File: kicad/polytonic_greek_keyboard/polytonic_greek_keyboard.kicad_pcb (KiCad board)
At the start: 2 copper layers, 34 parts, among them J1 PINHD_1x4_Male, J2 USB_C_Receptacle, J3 PINHD_1x2_Male, Q1 S8050, SW1 SW_Wuerth_450301014042, SW2 RotaryEncoder_Switch_MP, SW4 SW_SP4T_NR01104, SW5 SW_SPST, U1 ESP32-S2-WROVER, U2 PCF8574T

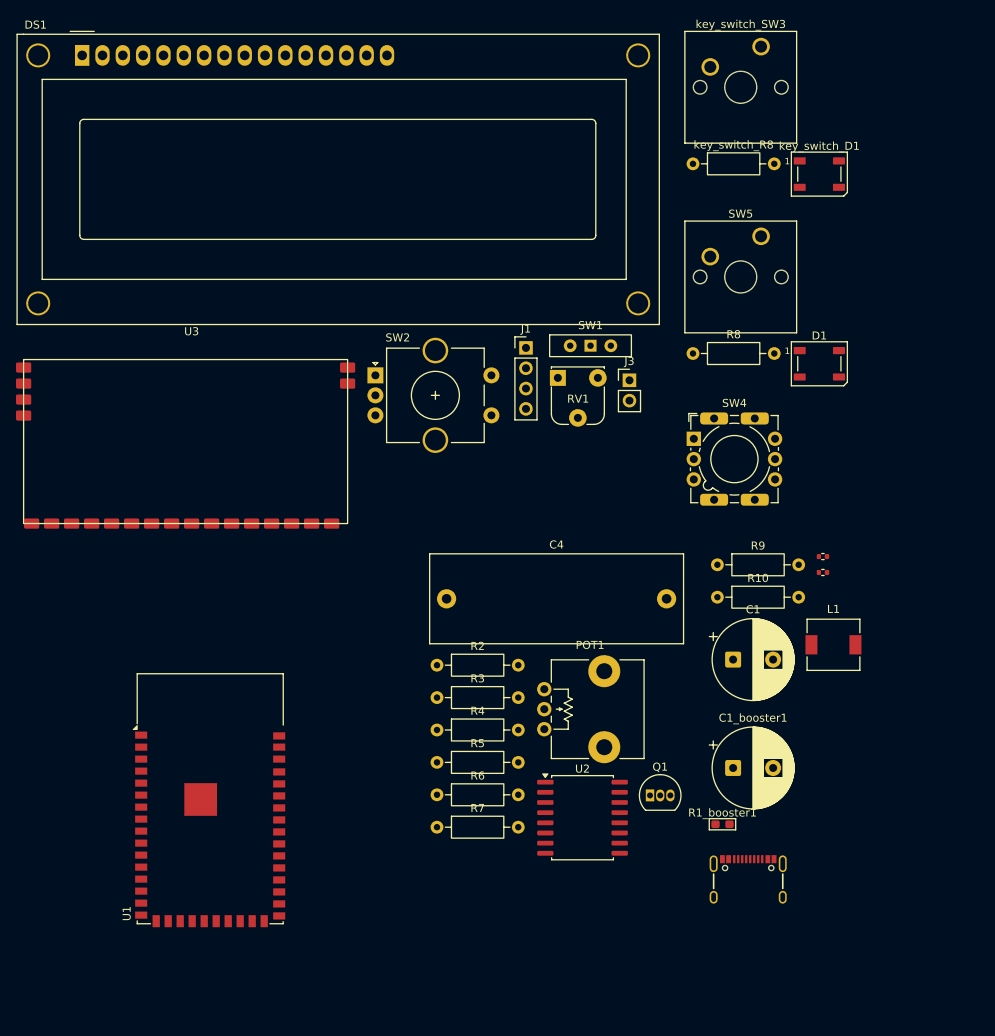
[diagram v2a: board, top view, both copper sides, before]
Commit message: [ADD] a more structured approach of the pcb in a way that won't overload the esp32 that is running it
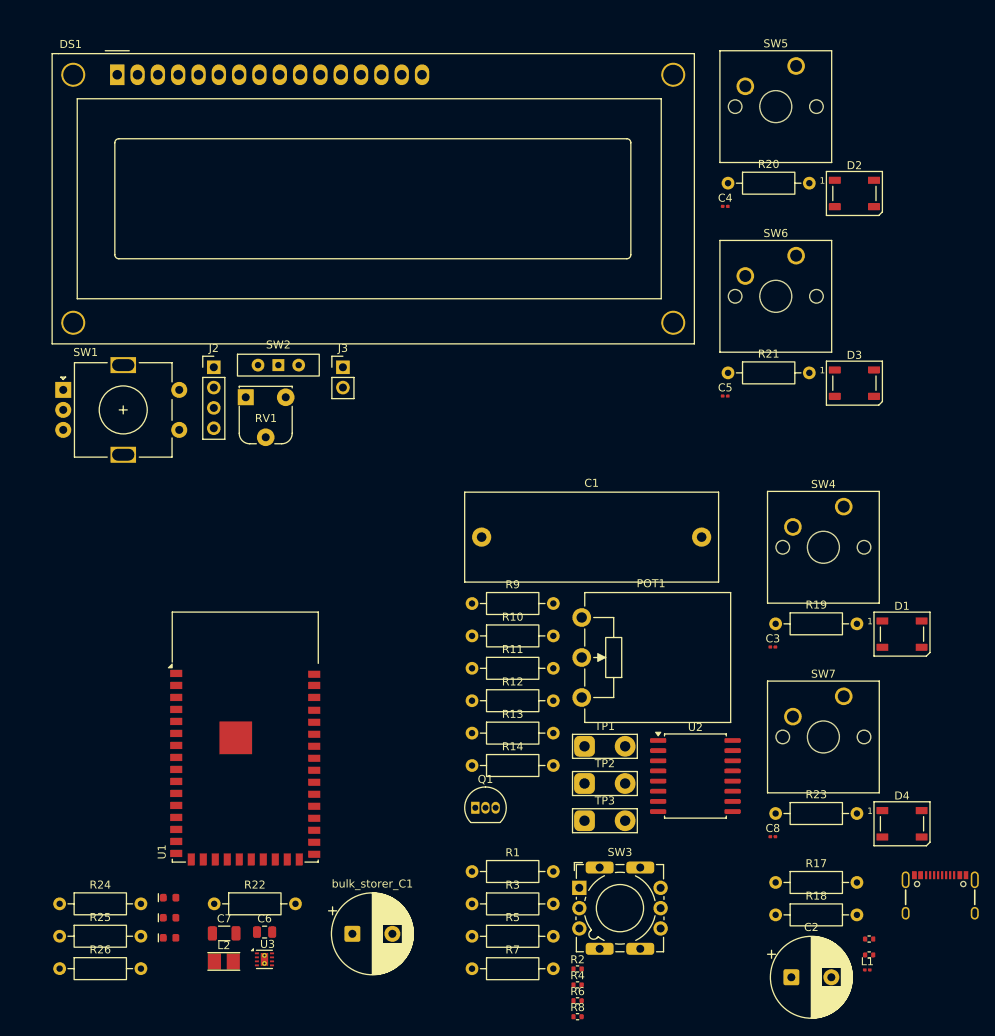
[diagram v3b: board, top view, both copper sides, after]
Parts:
- removed C1_booster1: 1000uF_16V, Capacitor_THT:CP_Radial_D10.0mm_P5.00mm
- removed R1_booster1: 330R_0603, PCM_Resistor_SMD_AKL:R_0603_1608Metric_Pad1.05x0.95mm_HandSolder
- removed key_switch_D1: WS2812B, LED_SMD:LED_WS2812B_PLCC4_5.0x5.0mm_P3.2mm
- removed key_switch_R8: 330ohm, Resistor_THT:R_Axial_DIN0207_L6.3mm_D2.5mm_P10.16mm_Horizontal
- removed key_switch_SW3: SW_SPST, Button_Switch_Keyboard:SW_Cherry_MX_1.00u_PCB
- added C2: 1000uF_16V, Capacitor_THT:CP_Radial_D10.0mm_P5.00mm, F.Cu at (114.1, 135.0)
- added C3: 0.1uF_0603_16V, Capacitor_SMD:C_0201_0603Metric, F.Cu at (111.8, 93.7)
- added C5: 0.1uF_0603_16V, Capacitor_SMD:C_0201_0603Metric, F.Cu at (105.8, 62.4)
- added C6: 10uF_0805_16V_lowESR, Capacitor_SMD:C_0805_2012Metric, F.Cu at (48.2, 129.4)
- added C7: 22uF_1206_25V, Capacitor_SMD:C_1206_3216Metric, F.Cu at (43.2, 129.5)
- added C8: 0.1uF_0603_16V, Capacitor_SMD:C_0201_0603Metric, F.Cu at (111.8, 117.4)
- added D2: WS2812B, LED_SMD:LED_WS2812B_PLCC4_5.0x5.0mm_P3.2mm, F.Cu at (122.0, 37.0)
- added D3: WS2812B, LED_SMD:LED_WS2812B_PLCC4_5.0x5.0mm_P3.2mm, F.Cu at (122.0, 60.7)
- added D4: WS2812B, LED_SMD:LED_WS2812B_PLCC4_5.0x5.0mm_P3.2mm, F.Cu at (127.9, 115.8)
- added D5: Green, PCM_SparkFun-LED:LED_0603_1608Metric_Green, F.Cu at (36.4, 125.1)
- added D6: Green, PCM_SparkFun-LED:LED_0603_1608Metric_Green, F.Cu at (36.4, 127.6)
- added D7: Green, PCM_SparkFun-LED:LED_0603_1608Metric_Green, F.Cu at (36.4, 130.1)
- added L2: 2.2uH_2.4A_2016, Inductor_SMD:L_Taiyo-Yuden_NR-20xx_HandSoldering, F.Cu at (43.1, 133.0)
- added R1: 330ohm, Resistor_THT:R_Axial_DIN0207_L6.3mm_D2.5mm_P10.16mm_Horizontal, F.Cu at (74.2, 121.8)
- added R13: 47k, Resistor_THT:R_Axial_DIN0207_L6.3mm_D2.5mm_P10.16mm_Horizontal, F.Cu at (74.2, 104.5)
- added R14: 47k, Resistor_THT:R_Axial_DIN0207_L6.3mm_D2.5mm_P10.16mm_Horizontal, F.Cu at (74.2, 108.5)
- added R15: 5.1k, PCM_SparkFun-Resistor:R_0402_1005Metric, F.Cu at (123.8, 130.2)
- added R16: 5.1k, PCM_SparkFun-Resistor:R_0402_1005Metric, F.Cu at (123.8, 132.2)
- added R17: 22ohm, Resistor_THT:R_Axial_DIN0207_L6.3mm_D2.5mm_P10.16mm_Horizontal, F.Cu at (112.1, 123.2)
- added R18: 22ohm, Resistor_THT:R_Axial_DIN0207_L6.3mm_D2.5mm_P10.16mm_Horizontal, F.Cu at (112.1, 127.2)
- added R19: 330ohm, Resistor_THT:R_Axial_DIN0207_L6.3mm_D2.5mm_P10.16mm_Horizontal, F.Cu at (112.1, 90.8)
- added R20: 330ohm, Resistor_THT:R_Axial_DIN0207_L6.3mm_D2.5mm_P10.16mm_Horizontal, F.Cu at (106.2, 35.7)
- added R21: 330ohm, Resistor_THT:R_Axial_DIN0207_L6.3mm_D2.5mm_P10.16mm_Horizontal, F.Cu at (106.2, 59.5)
- added R22: 100k, Resistor_THT:R_Axial_DIN0207_L6.3mm_D2.5mm_P10.16mm_Horizontal, F.Cu at (41.9, 125.8)
- added R23: 330ohm, Resistor_THT:R_Axial_DIN0207_L6.3mm_D2.5mm_P10.16mm_Horizontal, F.Cu at (112.1, 114.5)
- added R24: 68ohm, Resistor_THT:R_Axial_DIN0207_L6.3mm_D2.5mm_P10.16mm_Horizontal, F.Cu at (22.6, 125.8)
- added R25: 220ohm, Resistor_THT:R_Axial_DIN0207_L6.3mm_D2.5mm_P10.16mm_Horizontal, F.Cu at (22.6, 129.9)
- added R26: 68ohm, Resistor_THT:R_Axial_DIN0207_L6.3mm_D2.5mm_P10.16mm_Horizontal, F.Cu at (22.6, 133.9)
- added SW3: SW_SP4T_NR01104, Button_Switch_THT:SW_NKK_NR01, F.Cu at (87.6, 123.8)
- added SW6: SW_SPST, Button_Switch_Keyboard:SW_Cherry_MX_1.00u_PCB, F.Cu at (114.7, 44.8)
- added SW7: SW_SPST, Button_Switch_Keyboard:SW_Cherry_MX_1.00u_PCB, F.Cu at (120.6, 99.9)
- added TP1: TestPoint_2Pole, Misc:TestPoint_2Pads_Pitch5.08mm_Drill1.3mm, F.Cu at (88.2, 106.1)
- added TP2: TestPoint_2Pole, Misc:TestPoint_2Pads_Pitch5.08mm_Drill1.3mm, F.Cu at (88.2, 110.8)
- added TP3: TestPoint_2Pole, Misc:TestPoint_2Pads_Pitch5.08mm_Drill1.3mm, F.Cu at (88.2, 115.4)
- added bulk_storer_C1: 1000uF_16V, Capacitor_THT:CP_Radial_D10.0mm_P5.00mm, F.Cu at (59.2, 129.6)
- C1: value 1000uF_16V -> 0.1uF; footprint Capacitor_THT:CP_Radial_D10.0mm_P5.00mm -> Capacitor_THT:C_Rect_L31.5mm_W11.0mm_P27.50mm_MKS4
- C4: value 0.1uF -> 0.1uF_0603_16V; footprint Capacitor_THT:C_Rect_L31.5mm_W11.0mm_P27.50mm_MKS4 -> Capacitor_SMD:C_0201_0603Metric
- J1: value PINHD_1x4_Male -> USB_C_Receptacle; footprint Connector_PinHeader_2.54mm:PinHeader_1x04_P2.54mm_Vertical -> PCM_SparkFun-Connector:USB-C_16
- J2: value USB_C_Receptacle -> PINHD_1x4_Male; footprint PCM_SparkFun-Connector:USB-C_16 -> Connector_PinHeader_2.54mm:PinHeader_1x04_P2.54mm_Vertical
- L1: footprint Inductor_SMD:L_6.3x6.3_H3 -> Inductor_SMD:L_0201_0603Metric
- POT1: footprint PCM_Potentiometer_THT_US_AKL:Potentiometer_Alps_RK09L_Single_Vertical -> Misc:Potentiometer_Piher_PC-16_Single_Vertical
- R10, R9: value 22ohm -> 1k
- R11: value 5.1k -> 47k; footprint PCM_SparkFun-Resistor:R_0402_1005Metric -> Resistor_THT:R_Axial_DIN0207_L6.3mm_D2.5mm_P10.16mm_Horizontal
- R12: value 5.1k -> 1k; footprint PCM_SparkFun-Resistor:R_0402_1005Metric -> Resistor_THT:R_Axial_DIN0207_L6.3mm_D2.5mm_P10.16mm_Horizontal
- R2, R6: value 47k -> 10k_0402; footprint Resistor_THT:R_Axial_DIN0207_L6.3mm_D2.5mm_P10.16mm_Horizontal -> Resistor_SMD:R_0402_1005Metric
- R3, R5: value 1k -> 330ohm
- R4: value 1k -> 10k_0402; footprint Resistor_THT:R_Axial_DIN0207_L6.3mm_D2.5mm_P10.16mm_Horizontal -> Resistor_SMD:R_0402_1005Metric
- R7: value 47k -> 330ohm
- R8: value 330ohm -> 10k_0402; footprint Resistor_THT:R_Axial_DIN0207_L6.3mm_D2.5mm_P10.16mm_Horizontal -> Resistor_SMD:R_0402_1005Metric
- SW1: value SW_Wuerth_450301014042 -> RotaryEncoder_Switch_MP; footprint Button_Switch_THT:SW_Slide-03_Wuerth-WS-SLTV_10x2.5x6.4_P2.54mm -> Misc:RotaryEncoder_Alps_EC11E-Switch_Vertical_H20mm
- SW2: value RotaryEncoder_Switch_MP -> SW_Wuerth_450301014042; footprint Rotary_Encoder:RotaryEncoder_Alps_EC11E-Switch_Vertical_H20mm_CircularMountingHoles -> Button_Switch_THT:SW_Slide-03_Wuerth-WS-SLTV_10x2.5x6.4_P2.54mm
- SW4: value SW_SP4T_NR01104 -> SW_SPST; footprint Button_Switch_THT:SW_NKK_NR01 -> Button_Switch_Keyboard:SW_Cherry_MX_1.00u_PCB
- U3: value ~ -> TPS62162DSG; footprint polytonic_greek_keyboard:I²C -> Package_SON:WSON-8-1EP_2x2mm_P0.5mm_EP0.9x1.6mm_ThermalVias
- moved J2 90.6 mm to (41.9, 58.8)
- moved R8 84.1 mm to (87.4, 139.9)
- moved J1 83.5 mm to (132.7, 121.9)
- moved U3 78.5 mm to (48.2, 132.8)
- moved SW1 66.1 mm to (23.1, 61.6)
- moved C4 60.2 mm to (105.8, 38.6)
- moved R12 46.7 mm to (74.2, 100.4)
- moved R11 46.0 mm to (74.2, 96.4)
- moved R2 41.8 mm to (87.4, 134.0)
- moved L1 40.9 mm to (123.6, 134.1)
- moved RV1 39.1 mm to (48.4, 64.5)
- moved R4 36.4 mm to (87.4, 136.0)
- moved J3 35.9 mm to (58.0, 58.8)
- moved D1 35.3 mm to (127.9, 92.1)
- moved C1 35.0 mm to (75.4, 80.0)
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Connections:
- net /key_alpha/switch_column renamed /key_matrix/Alphabet keys/col1_IN
- net /logic/ID01 renamed /key_matrix/row8_IN
- net /logic/ID03 renamed /key_matrix/row6_IN
- net /logic/ID04 renamed /key_matrix/row5_IN
- net /logic/ID05 renamed /key_matrix/row4_IN
- net /logic/ID06 renamed /key_matrix/row3_IN
- net /logic/ID07 renamed /key_matrix/row2_IN
- net /logic/ID08 renamed /key_matrix/row1_IN
- net /system_speech/VSS - LINUX renamed /key_matrix/Return/swt_col
- C1 pad 1: /power_filter/GND_IN -> VCC
- C1 pad 2: /power_filter/VBUS_OUT -> GND
- C4 pad 1: VCC -> /esp_voltage_stepdown/VDD_CLEAN
- C4 pad 2: GND -> Net-(D2-VDD)
- D1 pad 2: /key_alpha/LED_DOUT -> /key_matrix/Navigation keys/LED_DIN_IN
- D1 pad 3: /key_alpha/LED_VSS -> GND
- DS1 pad 1: Net-(DS1-VSS) -> GND
- DS1 pad 10: unconnected-(DS1-D3-Pad10) -> /display/Onboard_I2c/DB3
- DS1 pad 11: Net-(DS1-D4) -> /display/Onboard_I2c/DB4
- DS1 pad 12: Net-(DS1-D5) -> /display/Onboard_I2c/DB5
- DS1 pad 13: Net-(DS1-D6) -> /display/Onboard_I2c/DB6
- DS1 pad 14: Net-(DS1-D7) -> /display/Onboard_I2c/DB7
- DS1 pad 15: Net-(DS1-LED(+)) -> GND
- DS1 pad 16: Net-(DS1-LED(-)) -> /display/Onboard_I2c/(K) BL-
- DS1 pad 2: Net-(DS1-VDD) -> VCC
- DS1 pad 3: Net-(DS1-VO) -> /display/Onboard_I2c/V0
- DS1 pad 4: Net-(DS1-RS) -> /display/Onboard_I2c/RS
- DS1 pad 5: Net-(DS1-R/W) -> /display/Onboard_I2c/R/W
- DS1 pad 6: Net-(DS1-E) -> /display/Onboard_I2c/E
- DS1 pad 7: unconnected-(DS1-D0-Pad7) -> /display/Onboard_I2c/DB0
- DS1 pad 8: unconnected-(DS1-D1-Pad8) -> /display/Onboard_I2c/DB1
- DS1 pad 9: unconnected-(DS1-D2-Pad9) -> /display/Onboard_I2c/DB2
- J3 pad 2: Net-(U3-LED_VCC) -> VCC
- L1 pad 1: /power_filter/GND_IN -> GND
- L1 pad 2: /power_filter/VBUS_OUT -> /esp_voltage_stepdown/VDD_CLEAN
- R10 pad 1: /power_filter/DATA-_IN -> VCC
- R10 pad 2: /power_filter/DATA-_OUT -> /display/Onboard_I2c/A1
- R11 pad 1: /power_filter/CC1_IN -> /display/SDA
- R11 pad 2: /power_filter/GND_IN -> VCC
- R12 pad 1: /power_filter/CC2_IN -> VCC
- R12 pad 2: /power_filter/GND_IN -> /display/Onboard_I2c/A2
- R2 pad 1: VCC -> /logic/ID41
- R2 pad 2: Net-(Q1-B) -> /display/VCC_SCREEN
- R3 pad 1: VCC -> Net-(R3-Pad1)
- R3 pad 2: /display/Onboard_I2c/A0 -> /logic/ID45
- R4 pad 1: VCC -> /logic/ID45
- R4 pad 2: /display/Onboard_I2c/A1 -> /display/VCC_SCREEN
- R5 pad 1: VCC -> /logic/ID46
- R5 pad 2: /display/Onboard_I2c/A2 -> Net-(R5-Pad2)
- R6 pad 1: /display/Onboard_I2c/SCL -> /logic/ID46
- R6 pad 2: VCC -> /display/VCC_SCREEN
- R7 pad 1: /display/Onboard_I2c/SDA -> /logic/ID42
- R7 pad 2: VCC -> Net-(R7-Pad2)
- R8 pad 1: Net-(D1-DIN) -> /logic/ID42
- R8 pad 2: /key_alpha/LED_DIN -> /display/VCC_SCREEN
- R9 pad 1: /power_filter/DATA+_IN -> VCC
- R9 pad 2: /power_filter/DATA+_OUT -> /display/Onboard_I2c/A0
- RV1 pad 1: Net-(U3-LED_VCC) -> VCC
- RV1 pad 3: Net-(SW1-C) -> VCC
- SW4 pad 1: /system_speech/VSS - RAW -> /key_matrix/row7_IN
- SW5 pad 1: /key_alpha/switch_row -> /key_matrix/row9_IN
- U1 pad 1: /logic/GND -> GND
- U1 pad 12: /logic/ID09 -> /key_matrix/LED_DIN
- U1 pad 13: /logic/ID10 -> /display/SDA
- U1 pad 14: /logic/ID11 -> /display/SCL
- U1 pad 2: /logic/3v3 -> /display/VCC_SCREEN
- U1 pad 26: /logic/GND -> GND
- U1 pad 3: /logic/ID00 -> /key_matrix/row9_IN
- U1 pad 42: /logic/GND -> GND
- U1 pad 43: /logic/GND -> GND
- U1 pad 5: /logic/ID02 -> /key_matrix/row7_IN
- U2 pad 1: /display/Onboard_I2c/A0 -> unconnected-(U2-A0-Pad1)
- U2 pad 10: /display/Onboard_I2c/DB5 -> /display/Onboard_I2c/DB4
- U2 pad 11: /display/Onboard_I2c/DB6 -> /display/Onboard_I2c/DB5
- U2 pad 12: /display/Onboard_I2c/DB7 -> /display/Onboard_I2c/DB6
- U2 pad 14: /display/Onboard_I2c/SCL -> unconnected-(U2-SCL-Pad14)
- U2 pad 15: /display/Onboard_I2c/SDA -> /display/SCL
- U2 pad 2: /display/Onboard_I2c/A1 -> /display/Onboard_I2c/A0
- U2 pad 3: /display/Onboard_I2c/A2 -> /display/Onboard_I2c/A1
- U2 pad 4: /display/Onboard_I2c/RS -> unconnected-(U2-P0-Pad4)
- U2 pad 5: /display/Onboard_I2c/R/W -> /display/Onboard_I2c/RS
- U2 pad 6: /display/Onboard_I2c/E -> /display/Onboard_I2c/R/W
- U2 pad 7: Net-(Q1-B) -> /display/Onboard_I2c/E
- U2 pad 8: GND -> unconnected-(U2-GND-Pad8)
- U2 pad 9: /display/Onboard_I2c/DB4 -> Net-(Q1-B)
- U3 pad 2: Net-(DS1-VDD) -> GND
- U3 pad 3: /display/SDA -> GND
- U3 pad 4: /display/SCL -> GND
- U3 pad 5: Net-(DS1-R/W) -> GND
- U3 pad 7: unconnected-(U3-DB0-Pad7) -> Net-(U3-SW)
- U3 pad 8: unconnected-(U3-DB1-Pad8) -> Net-(U3-PG)
- U3 pad 9: unconnected-(U3-DB2-Pad9) -> GND

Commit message: [UPDATE] the board desing, [FIX] connection issues
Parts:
- added C9: 100nF_Ceramic, Capacitor_THT:C_Disc_D5.0mm_W2.5mm_P2.50mm, F.Cu at (75.2, 93.7)
- added D8: Blue, PCM_SparkFun-LED:LED_1206_3216Metric_Blue, F.Cu at (181.4, 132.2)
- added J4: Conn_01x11_Socket, Connector_PinSocket_2.00mm:PinSocket_1x11_P2.00mm_Horizontal, F.Cu at (197.5, 102.5)
- added J5: Conn_01x11_Pin, Connector_PinHeader_2.00mm:PinHeader_1x11_P2.00mm_Horizontal, F.Cu at (180.6, 102.5)
- added R27: 10k_0402, Resistor_SMD:R_0402_1005Metric, F.Cu at (81.2, 92.6)
- added R28: 10k_0402, Resistor_SMD:R_0402_1005Metric, F.Cu at (81.2, 94.6)
- added R29: 1k, Resistor_THT:R_Axial_DIN0207_L6.3mm_D2.5mm_P10.16mm_Horizontal, F.Cu at (180.2, 128.6)
- added SW8: Push_Button, Button_Switch_THT:SW_PUSH_6mm, F.Cu at (75.2, 76.6)
- added SW9: Push_Button, Button_Switch_THT:SW_PUSH_6mm, F.Cu at (75.2, 85.1)
- added U4: MCP23017_SP, Package_DIP:DIP-28_W7.62mm, F.Cu at (108.8, 21.5)
- added U5: MCP23017_SP, Package_DIP:DIP-28_W7.62mm, F.Cu at (119.5, 21.5)
- C3, C4, C5, C8: footprint Capacitor_SMD:C_0201_0603Metric -> Capacitor_SMD:C_0201_0603Metric_Pad0.64x0.40mm_HandSolder
- C6: footprint Capacitor_SMD:C_0805_2012Metric -> Capacitor_SMD:C_0805_2012Metric_Pad1.18x1.45mm_HandSolder
- C7: footprint Capacitor_SMD:C_1206_3216Metric -> Capacitor_SMD:C_1206_3216Metric_Pad1.33x1.80mm_HandSolder
- L1: footprint Inductor_SMD:L_0201_0603Metric -> Inductor_SMD:L_0201_0603Metric_Pad0.64x0.40mm_HandSolder
- POT1: footprint Misc:Potentiometer_Piher_PC-16_Single_Vertical -> Misc:Potentiometer_TT_P0915N
- TP1, TP2, TP3: footprint Misc:TestPoint_2Pads_Pitch5.08mm_Drill1.3mm -> Connector_PinHeader_2.00mm:PinHeader_1x02_P2.00mm_Horizontal
- moved DS1 168.8 mm to (198.4, 30.5)
- moved J3 162.4 mm to (218.5, 83.5)
- moved SW2 162.4 mm to (210.4, 83.2)
- moved J1 152.5 mm to (18.5, 20.8), turned to 180 degrees
- moved R26 108.0 mm to (108.8, 68.7)
- moved U3 108.0 mm to (134.4, 67.5)
- moved C6 108.0 mm to (134.4, 64.1)
- moved D5 108.0 mm to (122.5, 59.8)
- moved D6 108.0 mm to (122.5, 62.3)
- moved D7 108.0 mm to (122.5, 64.9)
- moved L2 108.0 mm to (129.3, 67.8)
- moved R24 108.0 mm to (108.8, 60.6)
- moved R25 108.0 mm to (108.8, 64.7)
- moved C7 108.0 mm to (129.3, 64.3)
- moved R22 108.0 mm to (128.1, 60.6)
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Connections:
- net /key_matrix/row2_IN renamed /logic/ID07
- net VCC renamed /display/Onboard_I2c/LED_VCC
- C1 pad 2: GND -> /display/GND
- C2 pad 1: GND -> /display/GND
- C3 pad 1: /esp_voltage_stepdown/VDD_CLEAN -> /key_matrix/VDD_IN
- C4 pad 1: /esp_voltage_stepdown/VDD_CLEAN -> /key_matrix/VDD_IN
- C5 pad 1: /esp_voltage_stepdown/VDD_CLEAN -> /key_matrix/VDD_IN
- C6 pad 2: GND -> /display/GND
- C7 pad 2: GND -> /display/GND
- C8 pad 1: /esp_voltage_stepdown/VDD_CLEAN -> /key_matrix/VDD_IN
- D1 pad 3: GND -> /key_matrix/VSS_IN
- D2 pad 3: GND -> /key_matrix/VSS_IN
- D3 pad 3: GND -> /key_matrix/VSS_IN
- D4 pad 3: GND -> /key_matrix/VSS_IN
- D5 pad 2: GND -> /display/GND
- D6 pad 2: GND -> /display/GND
- D7 pad 2: GND -> /display/GND
- DS1 pad 1: GND -> /display/GND
- DS1 pad 15: GND -> /display/GND
- J1 pad GND: GND -> /display/GND
- J1 pad S: GND -> /display/GND
- J1 pad VBUS: GND -> /display/GND
- J2 pad 1: GND -> /display/GND
- J3 pad 1: GND -> /display/GND
- L1 pad 1: GND -> /display/GND
- POT1 pad 3: GND -> /display/GND
- Q1 pad 1: GND -> /display/GND
- R1 pad 2: /logic/ID41 -> /logic/ID39
- R15 pad 2: GND -> /display/GND
- R16 pad 2: GND -> /display/GND
- R2 pad 1: /logic/ID41 -> /logic/ID39
- R24 pad 1: /logic/ID39 -> /logic/ID37
- R26 pad 1: /logic/ID40 -> /logic/ID38
- R3 pad 2: /logic/ID45 -> /logic/ID41
- R4 pad 1: /logic/ID45 -> /logic/ID41
- R5 pad 1: /logic/ID46 -> /logic/ID42
- R6 pad 1: /logic/ID46 -> /logic/ID42
- R7 pad 1: /logic/ID42 -> /logic/ID40
- R8 pad 1: /logic/ID42 -> /logic/ID40
- SW1 pad A: unconnected-(SW1-PadA) -> /display/GPIO_A
- SW1 pad B: unconnected-(SW1-PadB) -> /display/GPIO_B
- SW1 pad C: unconnected-(SW1-PadC) -> /display/GND
- SW1 pad S2: /display/SW1_OUT -> /display/GND
- SW2 pad 3: GND -> /display/GND
- SW3 pad C: GND -> /display/GND
- TP1 pad 2: GND -> /display/GND
- TP2 pad 2: GND -> /display/GND
- TP3 pad 2: GND -> /display/GND
- U1 pad 1: GND -> /display/GND
- U1 pad 11: /key_matrix/row1_IN -> /logic/ID08
- U1 pad 12: /key_matrix/LED_DIN -> /logic/ID09
- U1 pad 13: /display/SDA -> /logic/ID10
- U1 pad 14: /display/SCL -> /logic/ID11
- U1 pad 25: /logic/ID26 -> /display/GPIO_B
- U1 pad 26: GND -> /display/GND
- U1 pad 27: /logic/ID33 -> /display/GPIO_A
- U1 pad 28: /logic/ID34 -> /display/SW1_IN
- U1 pad 29: /logic/ID35 -> /display/SCL
- U1 pad 3: /key_matrix/row9_IN -> Net-(U1-IO00)
- U1 pad 30: /logic/ID36 -> /display/SDA
- U1 pad 39: /logic/ID45 -> unconnected-(U1-IO45-Pad39)
- U1 pad 4: /key_matrix/row8_IN -> /logic/ID01
- U1 pad 40: /logic/ID46 -> unconnected-(U1-IO46-Pad40)
- U1 pad 41: /logic/EN -> Net-(U1-EN)
- U1 pad 42: GND -> /display/GND
- U1 pad 43: GND -> /display/GND
- U1 pad 5: /key_matrix/row7_IN -> /logic/ID02
- U1 pad 6: /key_matrix/row6_IN -> /logic/ID03
- U1 pad 7: /key_matrix/row5_IN -> /logic/ID04
- U1 pad 8: /key_matrix/row4_IN -> /logic/ID05
- U1 pad 9: /key_matrix/row3_IN -> /logic/ID06
- U2 pad 1: unconnected-(U2-A0-Pad1) -> /display/Onboard_I2c/A0
- U2 pad 10: /display/Onboard_I2c/DB4 -> /display/Onboard_I2c/DB5
- U2 pad 11: /display/Onboard_I2c/DB5 -> /display/Onboard_I2c/DB6
- U2 pad 12: /display/Onboard_I2c/DB6 -> /display/Onboard_I2c/DB7
- U2 pad 14: unconnected-(U2-SCL-Pad14) -> /display/SCL
- U2 pad 15: /display/SCL -> /display/SDA
- U2 pad 2: /display/Onboard_I2c/A0 -> /display/Onboard_I2c/A1
- U2 pad 3: /display/Onboard_I2c/A1 -> /display/Onboard_I2c/A2
- U2 pad 4: unconnected-(U2-P0-Pad4) -> /display/Onboard_I2c/RS
- U2 pad 5: /display/Onboard_I2c/RS -> /display/Onboard_I2c/R/W
- U2 pad 6: /display/Onboard_I2c/R/W -> /display/Onboard_I2c/E
- U2 pad 7: /display/Onboard_I2c/E -> Net-(Q1-B)
- U2 pad 8: unconnected-(U2-GND-Pad8) -> /display/GND
- U2 pad 9: Net-(Q1-B) -> /display/Onboard_I2c/DB4
- U3 pad 1: GND -> /display/GND
- U3 pad 2: GND -> /display/GND
- U3 pad 3: GND -> /display/GND
- U3 pad 4: GND -> /display/GND
- U3 pad 5: GND -> /display/GND
- U3 pad 6: GND -> /display/GND
- U3 pad 9: GND -> /display/GND
- bulk_storer_C1 pad 1: GND -> /key_matrix/VSS_IN
- bulk_storer_C1 pad 2: /esp_voltage_stepdown/VDD_CLEAN -> /key_matrix/VDD_IN
